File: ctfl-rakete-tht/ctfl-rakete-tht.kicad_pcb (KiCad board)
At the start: 2 copper layers, 99.8 x 99.4 mm, 21 parts, among them J1 Conn_02x03_Odd_Even, SW1 SW_SPDT, U1 ATtiny212-SS

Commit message: optimized switch connections
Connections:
- SW1 pad 2: Net-(BT1-+) -> +3V0
- SW1 pad 3: +3V0 -> Net-(BT1-+)
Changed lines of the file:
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@@
 		(tags "BC-2001 CR2032 2032 Battery Holder")
 		(property "Reference" "BT1"
-			(at 0 -11.5 135)
+			(at 0 7.778175 135)
 			(layer "B.SilkS")
 			(effects
@@
 		(tags "switch spdt")
 		(property "Reference" "SW1"
-			(at 0 4.800001 -45)
+			(at 0 -2.828427 -45)
 			(layer "B.SilkS")
 			(effects
@@
 			(layers "B.Cu" "B.Paste" "B.Mask")
 			(roundrect_rratio 0.2)
-			(net 2 "Net-(BT1-+)")
+			(net 3 "+3V0")
 			(pinfunction "B")
 			(pintype "passive")
@@
 			(layers "B.Cu" "B.Paste" "B.Mask")
 			(roundrect_rratio 0.2)
-			(net 3 "+3V0")
+			(net 2 "Net-(BT1-+)")
 			(pinfunction "C")
 			(pintype "passive")

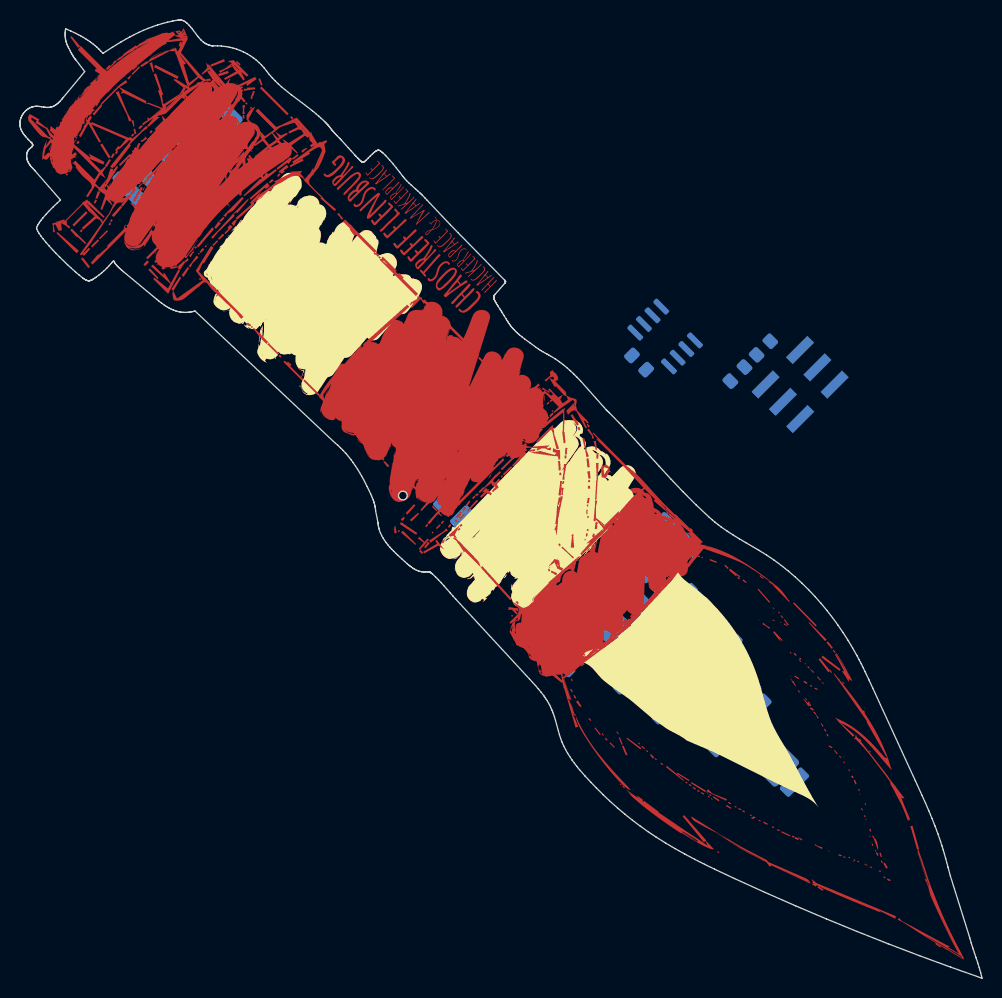
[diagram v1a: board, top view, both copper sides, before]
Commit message: placed other components and started routing
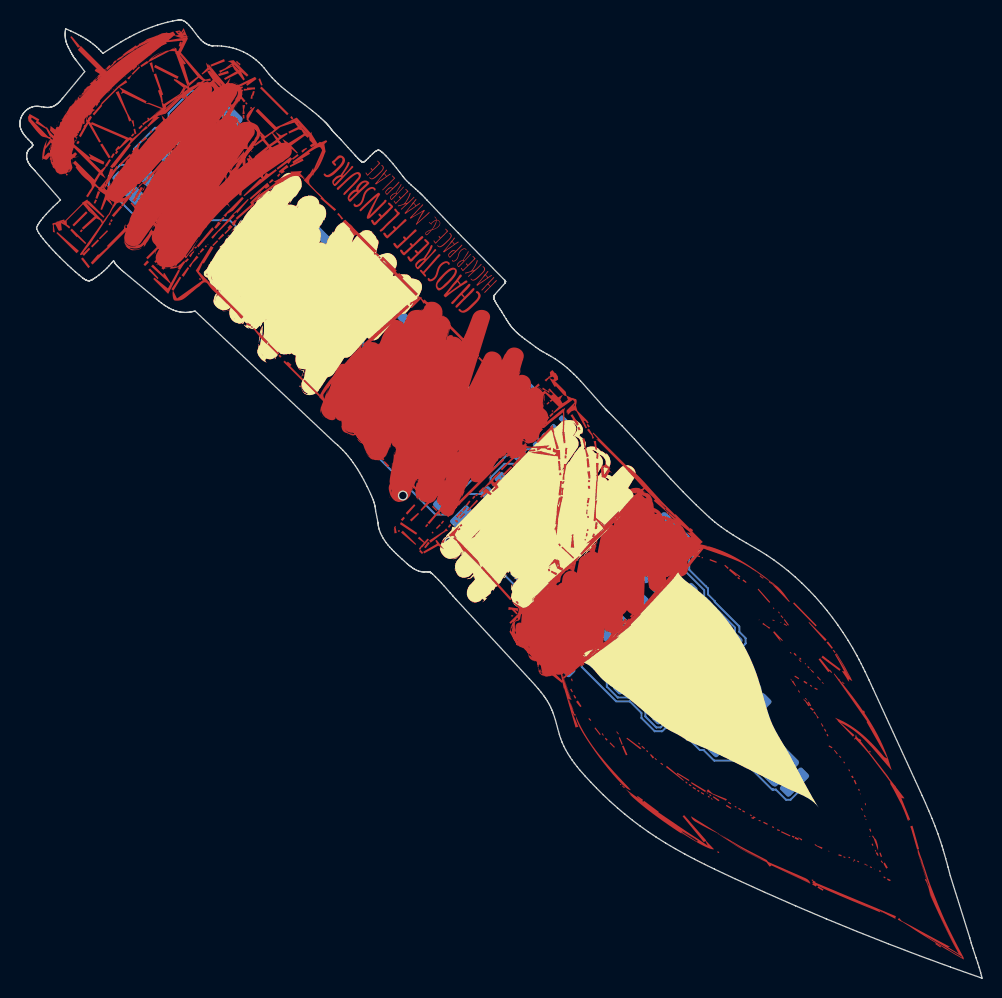
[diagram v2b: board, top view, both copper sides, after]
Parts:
- moved J1 31.8 mm to (154.2, 105.1)
- moved R1 30.7 mm to (151.1, 100.3)
- moved C2 27.7 mm to (149.4, 98.6)
- moved C1 15.8 mm to (151.0, 94.3)
- moved U1 15.8 mm to (153.7, 91.6)
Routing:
- net GND: track 0.00 -> 210.4 mm
- net /flame_outer: track 0.00 -> 74.0 mm
- net /flame_inner: track 0.00 -> 43.9 mm
- net Net-(BT1-+): track 0.00 -> 37.5 mm
- net +3V0: track 0.00 -> 33.9 mm
- net /UPDI_DATA: track 0.00 -> 14.4 mm
- net /light_right: track 0.00 -> 3.04 mm
- net /light_center: track 0.00 -> 3.04 mm
- net /light_left: track 0.00 -> 3.04 mm

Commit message: finished layout for revision A
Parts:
- added JP1: SolderJumper_2_Open, Jumper:SolderJumper-2_P1.3mm_Open_RoundedPad1.0x1.5mm, B.Cu at (146.5, 93.5)
- added JP2: SolderJumper_2_Open, Jumper:SolderJumper-2_P1.3mm_Open_RoundedPad1.0x1.5mm, B.Cu at (150.3, 86.2)
- added JP3: SolderJumper_2_Open, Jumper:SolderJumper-2_P1.3mm_Open_RoundedPad1.0x1.5mm, B.Cu at (148.5, 84.4)
- added JP4: SolderJumper_2_Open, Jumper:SolderJumper-2_P1.3mm_Open_RoundedPad1.0x1.5mm, B.Cu at (146.7, 82.6)
- added JP5: SolderJumper_2_Open, Jumper:SolderJumper-2_P1.3mm_Open_RoundedPad1.0x1.5mm, B.Cu at (158.8, 94.7)
- added JP6: SolderJumper_2_Open, Jumper:SolderJumper-2_P1.3mm_Open_RoundedPad1.0x1.5mm, B.Cu at (160.6, 96.5)
- SW1: footprint Button_Switch_SMD:SW_SPDT_CK_JS102011SAQN -> local:SW_SPDT_ESP4020
- moved SW1 3.31 mm to (142.0, 98.6)
- moved BT1 2.83 mm to (133.7, 78.7)
- moved C1 0.28 mm to (150.8, 94.1)
- moved U1 0.28 mm to (153.5, 91.4)
- moved D1 0.05 mm to (111.2, 65.9)
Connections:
- U1 pad 2: /flame_inner -> /light_left
- U1 pad 3: /flame_outer -> /light_center
- U1 pad 4: /light_left -> /light_right
- U1 pad 5: /light_center -> /flame_outer
- U1 pad 7: /light_right -> /flame_inner
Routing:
- net /light_left: track 3.04 -> 65.0 mm
- net /light_center: track 3.04 -> 62.4 mm
- net /light_right: track 3.04 -> 49.3 mm
- net /flame_inner: track 43.9 -> 72.5 mm
- net +3V0: track 33.9 -> 58.5 mm
- net /flame_outer: track 74.0 -> 92.1 mm
- net GND: track 210.4 -> 211.8 mm
- net Net-(BT1-+): track 37.5 -> 38.4 mm
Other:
- board text added: "100n"
- board text added: "4k7"
- board text added: "ATTINY212"
- board text added: "CR2023"
- board text added: "GND"
- board text added: "LEDs on"
- board text added: "OFF"
- board text added: "ON"
- board text added: "PWR"
- board text added: "UPDI"
- board text added: "VCC"
- board text added: "ctfl-rakete (c) 05-2024 CC-BY-SA 4.0 Jost Salathé - Rev.A"

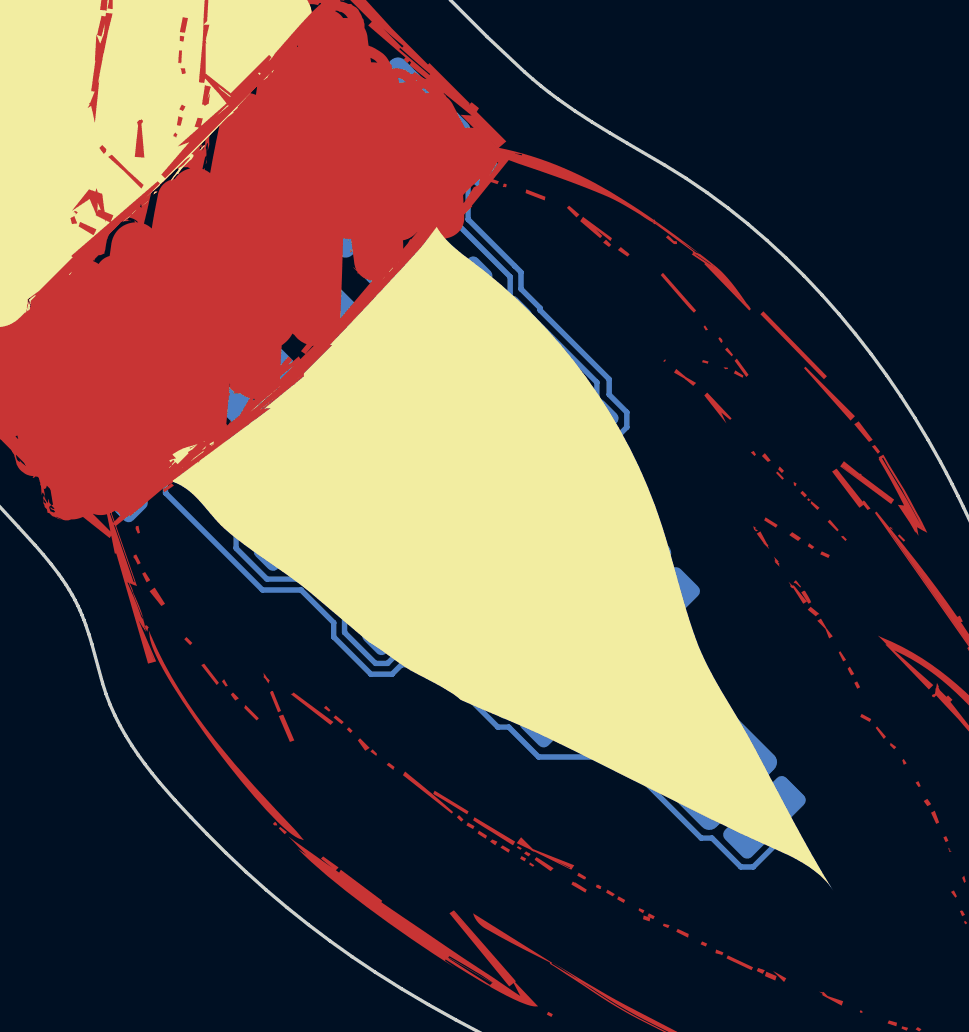
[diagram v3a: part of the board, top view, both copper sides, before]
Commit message: replaced in-flame LED footprints with 0805-only version and reoriented them
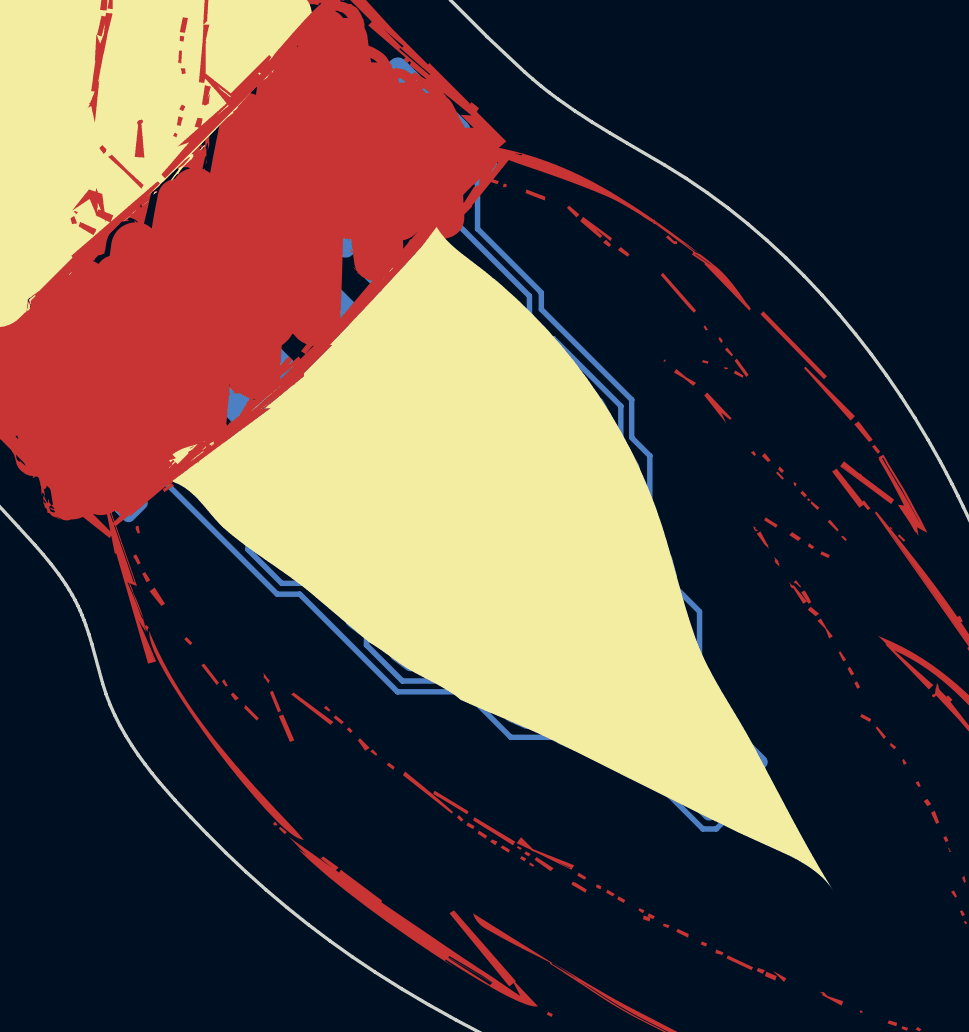
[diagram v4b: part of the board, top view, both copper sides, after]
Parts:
- D12, D13, D14, D6, D7, D8, D9: footprint local:LED_combo_0805_5mmSMD_HandSolder -> local:LED_0805_SMD_HandSolder
- moved D14 1.98 mm to (179.0, 127.8)
- moved D8 1.80 mm to (174.5, 115.4), turned to 119 degrees
- moved D9 1.14 mm to (166.6, 122.4), turned to -37 degrees
- moved D6 1.06 mm to (171.0, 110.9), turned to 136 degrees
- moved D13 0.63 mm to (172.5, 125.6), turned to -24 degrees
- moved D7 0.54 mm to (162.2, 118.8), turned to -40 degrees
- moved D12 0.42 mm to (176.7, 121.1), turned to 105 degrees
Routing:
- net GND: track 211.8 -> 196.7 mm
- net /flame_outer: track 92.1 -> 79.9 mm
- net /flame_inner: track 72.5 -> 65.2 mm
